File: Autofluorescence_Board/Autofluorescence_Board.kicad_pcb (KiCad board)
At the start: 2 copper layers, 19 parts, among them J1 Conn_01x04, J2 Conn_01x04, Q1 BSS138, Q2 A03401A, U1 PAM2863ECR

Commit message: Rearranged Layout
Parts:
- moved R4 5.95 mm to (147.0, 117.1), turned to -90 degrees
- moved D2 4.96 mm to (150.0, 115.0)
- moved C2 4.05 mm to (143.0, 117.1)
- moved C3 4.05 mm to (145.0, 117.1)
- moved Q2 3.49 mm to (147.0, 113.1)
- moved J1 2.05 mm to (138.0, 122.0)
- moved Q1 1.06 mm to (148.9, 108.0)
- moved R2 1.06 mm to (145.9, 108.0)
- moved J2 1.00 mm to (146.0, 102.0)
- moved C1 0.60 mm to (139.0, 115.0)
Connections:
- U1 pad 9: (no net) -> GND
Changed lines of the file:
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@@
 		(tags "SO exposed pad")
 		(property "Reference" "U1"
-			(at 0 3.302 0)
+			(at 3.396 3.302 0)
 			(layer "F.SilkS")
 			(effects
@@
 			(unit
 				(name "A")
-				(pins "1" "2" "3" "4" "EPAD" "8" "7" "6" "5")
+				(pins "1" "2" "3" "4" "9" "8" "7" "6" "5")
 			)
 		)
@@
 		)
 		(fp_text user "${REFERENCE}"
-			(at 0 0 0)
+			(at 0 -3.525 0)
 			(layer "F.Fab")
 			(effects
@@
 			(size 2.613 3.502)
 			(layers "F.Cu" "F.Mask" "F.Paste")
+			(net "GND")
+			(pinfunction "EPAD_9")
+			(pintype "unspecified")
 			(solder_paste_margin_ratio -0.2)
 		)
@@
 	(footprint "AF_Footprint:DR73"
 		(layer "F.Cu")
-		(at 130 114 -90)
+		(at 130 114.0028 -90)
 		(tags "DR73-101-R ")
 		(property "Reference" "L1"
@@
 			(polygon
 				(pts
-					(xy 133.7592 112.2982) (xy 133.7592 115.7018) (xy 126.2408 115.7018) (xy 126.2408 112.2982)
+					(xy 133.7592 112.301) (xy 133.7592 115.7046) (xy 126.2408 115.7046) (xy 126.2408 112.301)
 				)
 			)
@@
 	(footprint "Connector_JST:JST_PH_B4B-PH-K_1x04_P2.00mm_Vertical"
 		(layer "F.Cu")
-		(at 147 102 180)
+		(at 146 102 180)
 		(descr "JST PH series connector, B4B-PH-K (http://www.jst-mfg.com/product/pdf/eng/ePH.pdf)")
 		(tags "connector JST PH vertical")
@@
 	(footprint "Resistor_SMD:R_0603_1608Metric_Pad0.98x0.95mm_HandSolder"
 		(layer "F.Cu")
-		(at 147 108.0875 -90)
+		(at 145.9375 108.05 -90)
 		(descr "Resistor SMD 0603 (1608 Metric), square (rectangular) end terminal, IPC-7351 nominal with elongated pad for handsoldering. (Body size source: IPC-SM-782 page 72, https://www.pcb-3d.com/wordpress/wp-content/uploads/ipc-sm-782a_amendment_1_and_2.pdf)")
 		(tags "resistor handsolder")
@@
 	(footprint "Capacitor_SMD:C_0603_1608Metric_Pad1.08x0.95mm_HandSolder"
 		(layer "F.Cu")
-		(at 146 119.8625 -90)
+		(at 143 117.1375 -90)
 		(descr "Capacitor SMD 0603 (1608 Metric), square (rectangular) end terminal, IPC-7351 nominal with elongated pad for handsoldering. (Body size source: IPC-SM-782 page 76, https://www.pcb-3d.com/wordpress/wp-content/uploads/ipc-sm-782a_amendment_1_and_2.pdf)")
 		(tags "capacitor handsolder")
 		(property "Reference" "C2"
-			(at -3 0 90)
+			(at 2 0 90)
 			(layer "F.SilkS")
 			(effects
@@
 	(footprint "MRDT_Devices:SOD-123_ONS-L"
 		(layer "F.Cu")
-		(at 151 119.8625 -90)
+		(at 150 115 -90)
 		(tags "MMSZ5240BT1G ")
 		(property "Reference" "D2"
-			(at 0 -2 270)
+			(at -4 0 270)
 			(unlocked yes)
 			(layer "F.SilkS")
@@
 	(footprint "Capacitor_SMD:C_0603_1608Metric_Pad1.08x0.95mm_HandSolder"
 		(layer "F.Cu")
-		(at 148 119.8625 -90)
+		(at 145 117.1375 -90)
 		(descr "Capacitor SMD 0603 (1608 Metric), square (rectangular) end terminal, IPC-7351 nominal with elongated pad for handsoldering. (Body size source: IPC-SM-782 page 76, https://www.pcb-3d.com/wordpress/wp-content/uploads/ipc-sm-782a_amendment_1_and_2.pdf)")
 		(tags "capacitor handsolder")
 		(property "Reference" "C3"
-			(at -3 0 90)
+			(at 2 0 90)
 			(layer "F.SilkS")
 			(effects
@@
 	(footprint "Connector_JST:JST_PH_S4B-PH-K_1x04_P2.00mm_Horizontal"
 		(layer "F.Cu")
-		(at 136 121.55)
+		(at 138 122)
 		(descr "JST PH series connector, S4B-PH-K (http://www.jst-mfg.com/product/pdf/eng/ePH.pdf)")
 		(tags "connector JST PH horizontal")
 		(property "Reference" "J1"
-			(at 3 -3.138 0)
+			(at -3 0.45 0)
 			(layer "F.SilkS")
 			(effects
@@
 	(footprint "Package_TO_SOT_SMD:SOT-23"
 		(layer "F.Cu")
-		(at 150 108.0875)
+		(at 148.9375 108.05)
 		(descr "SOT, 3 Pin (JEDEC TO-236 Var AB https://www.jedec.org/document_search?search_api_views_fulltext=TO-236)")
 		(tags "SOT TO_SOT_SMD")
 		(property "Reference" "Q1"
-			(at 2 2 0)
+			(at 2 -2.05 0)
 			(layer "F.SilkS")
 			(effects
@@
 	(footprint "Resistor_SMD:R_0603_1608Metric_Pad0.98x0.95mm_HandSolder"
 		(layer "F.Cu")
-		(at 148 123 180)
+		(at 147 117.1375 -90)
 		(descr "Resistor SMD 0603 (1608 Metric), square (rectangular) end terminal, IPC-7351 nominal with elongated pad for handsoldering. (Body size source: IPC-SM-782 page 72, https://www.pcb-3d.com/wordpress/wp-content/uploads/ipc-sm-782a_amendment_1_and_2.pdf)")
 		(tags "resistor handsolder")
 		(property "Reference" "R4"
-			(at 0 -1.43 0)
+			(at 0 -1.43 90)
 			(layer "F.SilkS")
 			(effects
@@
 		)
 		(property "Value" "10K"
-			(at 0 1.43 0)
+			(at 0 1.43 90)
 			(layer "F.Fab")
 			(effects
@@
 		)
 		(property "Datasheet" ""
-			(at 0 0 0)
+			(at 0 0 90)
 			(layer "F.Fab")
 			(hide yes)
@@
 		)
 		(property "Description" "Resistor, US symbol"
-			(at 0 0 0)
+			(at 0 0 90)
 			(layer "F.Fab")
 			(hide yes)
@@
 		)
 		(property "KiLib_Generator" "SMD_2terminal_chip_molded"
-			(at 0 0 0)
+			(at 0 0 90)
 			(layer "F.SilkS")
 			(hide yes)
@@
 		)
 		(fp_text user "${REFERENCE}"
-			(at 0 0 0)
+			(at 0 0 90)
 			(layer "F.Fab")
 			(effects
@@
 		)
 		(pad "1" smd roundrect
-			(at -0.9125 0 180)
+			(at -0.9125 0 270)
 			(size 0.975 0.95)
 			(layers "F.Cu" "F.Mask" "F.Paste")
@@
 		)
 		(pad "2" smd roundrect
-			(at 0.9125 0 180)
+			(at 0.9125 0 270)
 			(size 0.975 0.95)
 			(layers "F.Cu" "F.Mask" "F.Paste")
@@
 		(tags "D_SOD-123F")
 		(property "Reference" "D1"
-			(at 0 -2.032 0)
+			(at -3 0 0)
 			(layer "F.SilkS")
 			(effects
@@
 		(tags "resistor handsolder")
 		(property "Reference" "R3"
-			(at 0 -1.65 90)
+			(at 1 1 90)
 			(layer "F.SilkS")
 			(effects
@@
 	(footprint "Package_TO_SOT_SMD:SOT-23"
 		(layer "F.Cu")
-		(at 149.95 114.925 90)
+		(at 147 113.0625 90)
 		(descr "SOT, 3 Pin (JEDEC TO-236 Var AB https://www.jedec.org/document_search?search_api_views_fulltext=TO-236)")
 		(tags "SOT TO_SOT_SMD")
@@
 	(footprint "Capacitor_SMD:C_1206_3216Metric_Pad1.33x1.80mm_HandSolder"
 		(layer "F.Cu")
-		(at 138.396 115 180)
+		(at 139 115 180)
 		(descr "Capacitor SMD 1206 (3216 Metric), square (rectangular) end terminal, IPC-7351 nominal with elongated pad for handsoldering. (Body size source: IPC-SM-782 page 76, https://www.pcb-3d.com/wordpress/wp-content/uploads/ipc-sm-782a_amendment_1_and_2.pdf)")
 		(tags "capacitor handsolder")

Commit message: Finalized Initial Layout
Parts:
- J2: footprint Connector_JST:JST_PH_B4B-PH-K_1x04_P2.00mm_Vertical -> Connector_JST:JST_PH_S4B-PH-K_1x04_P2.00mm_Horizontal
- moved H1 64.1 mm to (151.6, 126.0)
- moved H3 44.4 mm to (151.6, 98.0)
- moved H2 44.0 mm to (129.0, 126.0)
- moved H4 22.4 mm to (129.0, 98.0)
- moved J2 2.53 mm to (143.5, 101.9)
- moved L1 0.56 mm to (130.6, 114.0)
- moved J1 0.54 mm to (137.5, 122.0)
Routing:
- added copper zone on B.Cu, net GND
- added copper zone on F.Cu, net GND
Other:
- board outline added: 29.7 x 35.1 mm

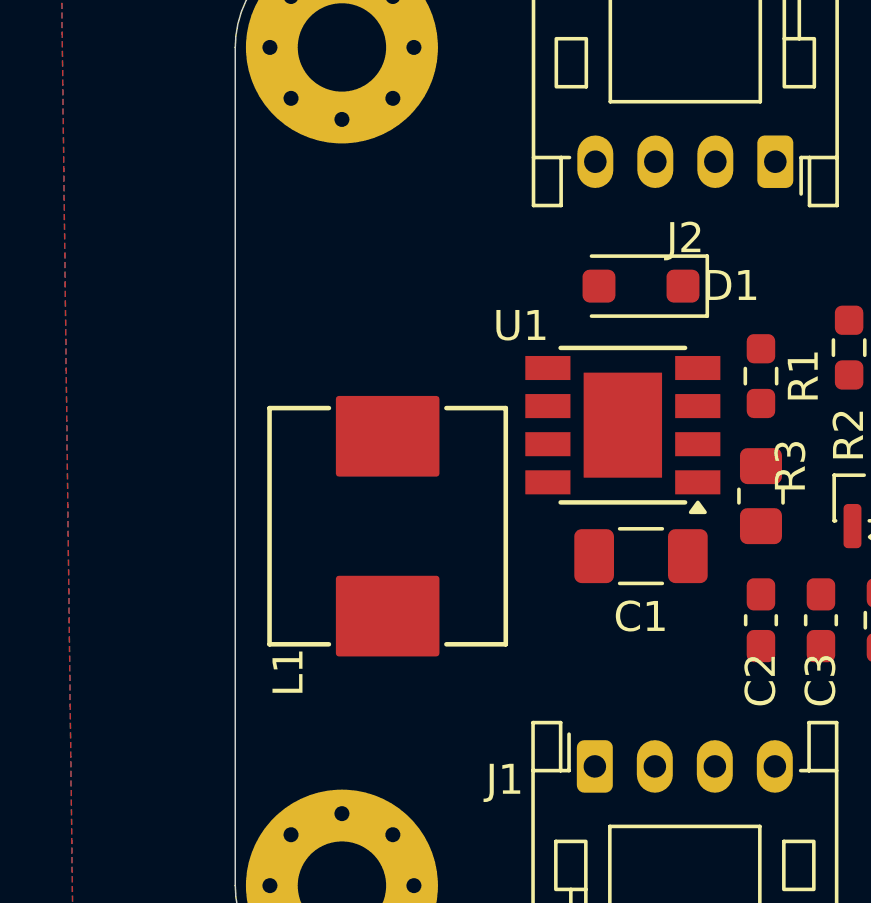
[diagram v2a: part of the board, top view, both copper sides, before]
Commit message: added fan connector, cause im a dumbass
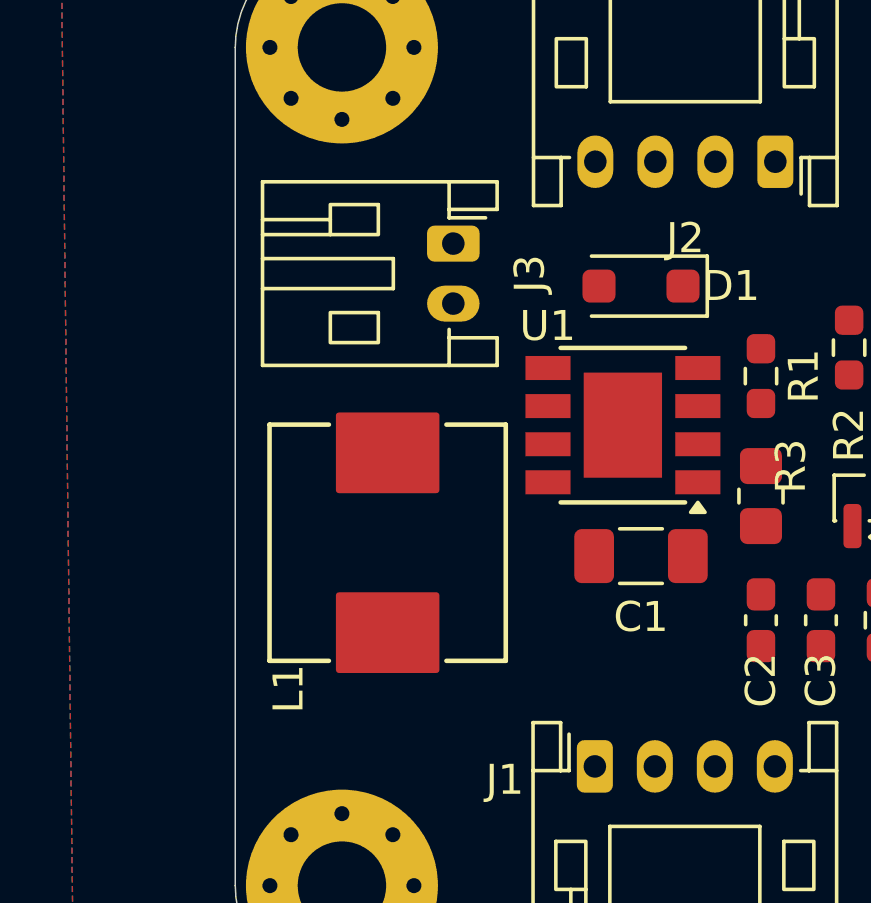
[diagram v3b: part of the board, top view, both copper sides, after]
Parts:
- added J3: Conn_01x02, Connector_JST:JST_PH_S2B-PH-K_1x02_P2.00mm_Horizontal, F.Cu at (132.7, 104.6)
- moved L1 0.55 mm to (130.6, 114.6)
